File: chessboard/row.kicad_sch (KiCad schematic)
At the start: 15 parts, among them U1 PCA9548ADB

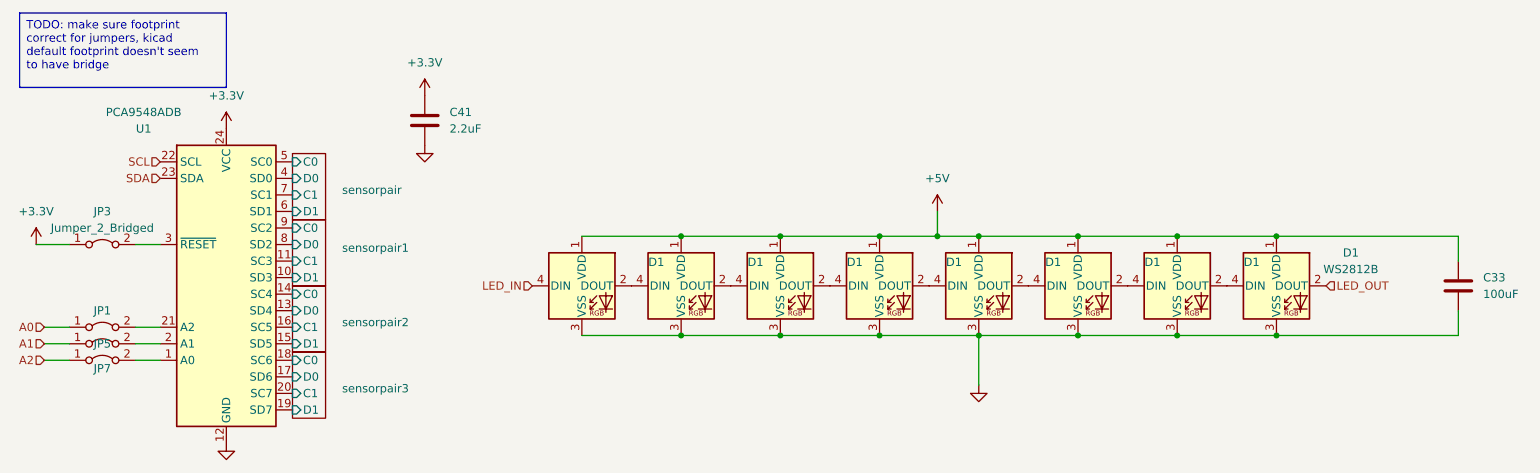
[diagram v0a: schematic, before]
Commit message: add some power logic, split chessboard and control board
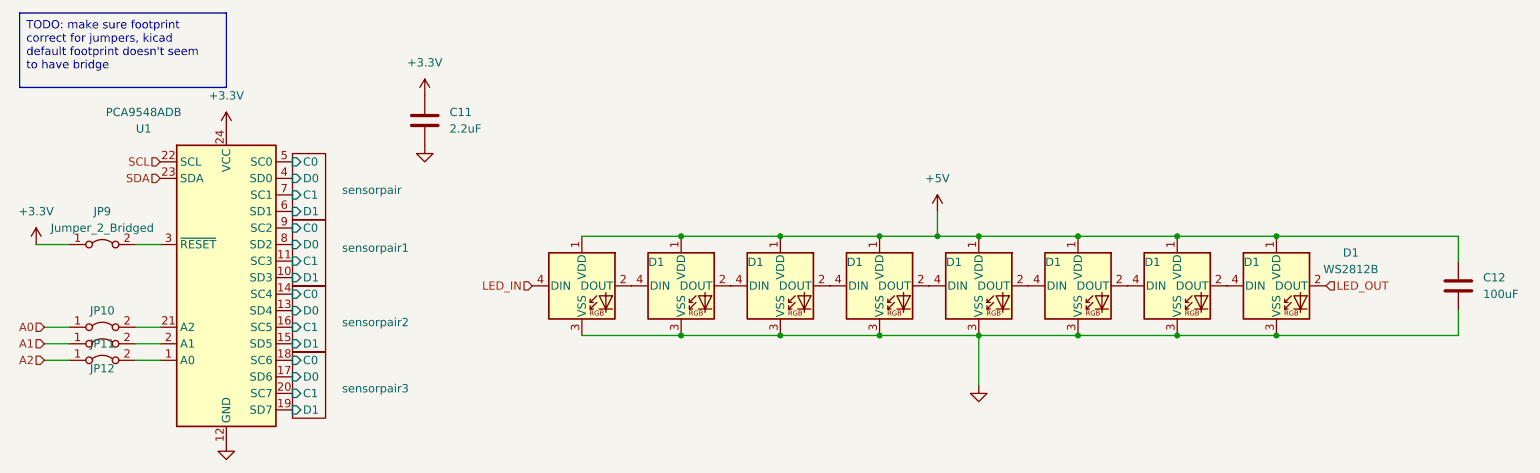
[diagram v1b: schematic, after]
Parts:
- renumbered C41 to C11, C33 to C12, JP1 to JP10, JP5 to JP11, JP7 to JP12, JP3 to JP9

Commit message: a
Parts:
- C3: renamed from C11; value 2.2uF -> 100nF; footprint (none) -> Capacitor_SMD:C_0805_2012Metric_Pad1.18x1.45mm_HandSolder
- C4: renamed from C12; value 100uF -> 22uF; footprint (none) -> Capacitor_SMD:C_0805_2012Metric_Pad1.18x1.45mm_HandSolder
- JP2: renamed from JP9; footprint (none) -> mylibrary:Bridged 2.5mm 1.0mm Test Points
- JP3: renamed from JP10; footprint (none) -> mylibrary:Bridged 2.5mm 1.0mm Test Points
- JP4: renamed from JP11; footprint (none) -> mylibrary:Bridged 2.5mm 1.0mm Test Points
- JP5: renamed from JP12; footprint (none) -> mylibrary:Bridged 2.5mm 1.0mm Test Points
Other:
- sheet sensorpair renamed sensorpair0

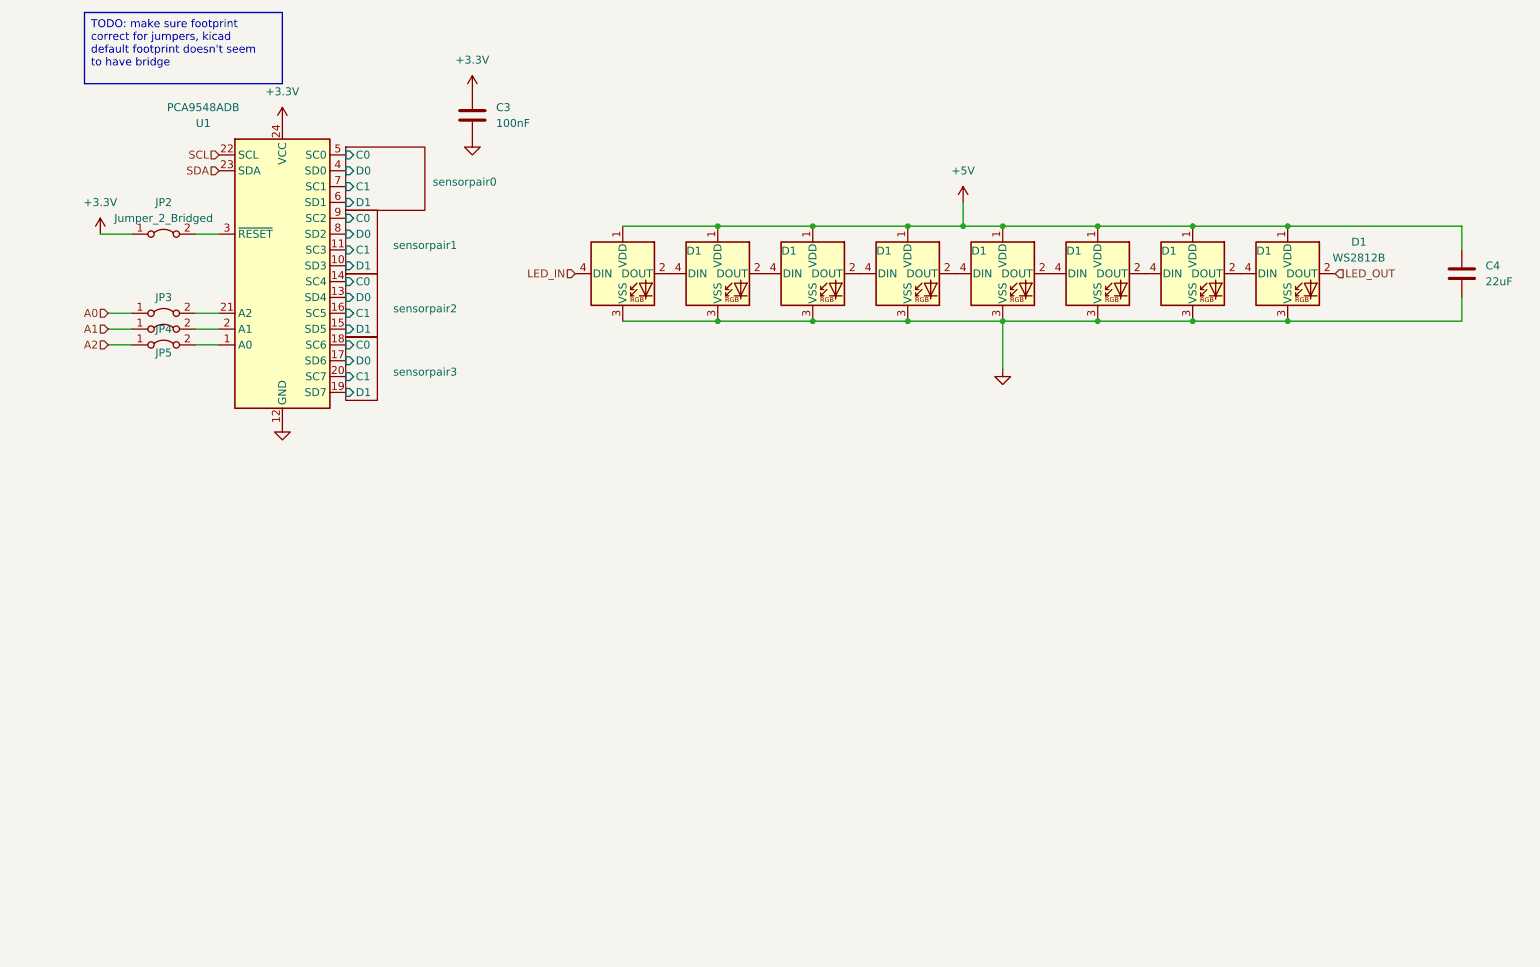
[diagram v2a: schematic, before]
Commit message: new single row board
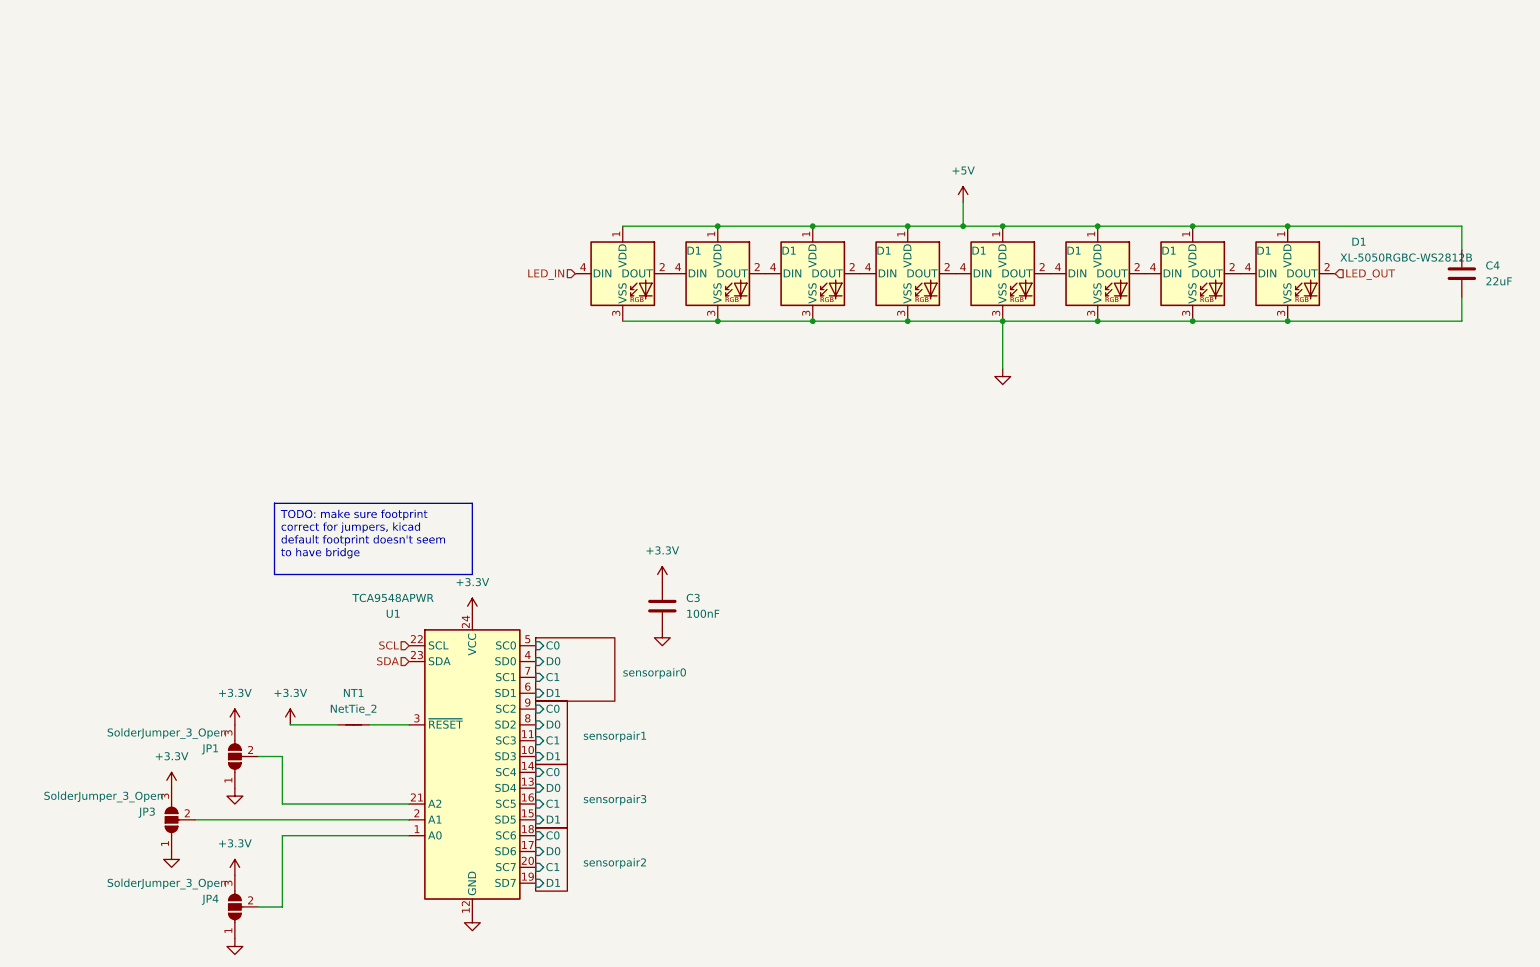
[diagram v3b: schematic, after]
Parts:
- removed JP2, JP3, JP4, JP5: Jumper_2_Bridged, mylibrary:Bridged 2.5mm 1.0mm Test Points, symbol Jumper:Jumper_2_Bridged
- added JP1, JP3, JP4: SolderJumper_3_Open, Jumper:SolderJumper-3_P2.0mm_Open_TrianglePad1.0x1.5mm, symbol Jumper:SolderJumper_3_Open
- added NT1: NetTie_2, Jumper:SolderJumper-2_P1.3mm_Bridged_Pad1.0x1.5mm, symbol Device:NetTie_2
- D1: value WS2812B -> XL-5050RGBC-WS2812B
- U1: value PCA9548ADB -> TCA9548APWR; footprint Package_SO:SSOP-24_5.3x8.2mm_P0.65mm -> Package_SO:TSSOP-24_4.4x7.8mm_P0.65mm
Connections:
- net +3.3V: now also JP1.3 (B), JP3.3 (B), JP4.3 (B), NT1.1
- net GND: now also JP1.1 (A), JP3.1 (A), JP4.1 (A)
- net sensorpair2/C0: now also U1.18 (SC6); no longer U1.14 (SC4)
- net sensorpair2/C1: now also U1.20 (SC7); no longer U1.16 (SC5)
- net sensorpair2/D0: now also U1.17 (SD6); no longer U1.13 (SD4)
- net sensorpair2/D1: now also U1.19 (SD7); no longer U1.15 (SD5)
- net sensorpair3/C0: now also U1.14 (SC4); no longer U1.18 (SC6)
- net sensorpair3/C1: now also U1.16 (SC5); no longer U1.20 (SC7)
- net sensorpair3/D0: now also U1.13 (SD4); no longer U1.17 (SD6)
- net sensorpair3/D1: now also U1.15 (SD5); no longer U1.19 (SD7)
- net at U1.1 (A0): now also JP4.2 (C)
- net at U1.2 (A1): now also JP3.2 (C)
- net at U1.21 (A2): now also JP1.2 (C)
- net at U1.3 (~{RESET}): now also NT1.2
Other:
- moved on the sheet: C3, U1

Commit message: make it pretty
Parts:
- renumbered C3 to C1, C4 to C2
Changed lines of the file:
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@@
   (symbol (lib_id "power:+3.3V") (at 120.65 116.84 0) (unit 1)
     (in_bom yes) (on_board yes) (dnp no) (fields_autoplaced)
-    (property "Reference" "#PWR037" (at 120.65 120.65 0)
+    (property "Reference" "#PWR019" (at 120.65 120.65 0)
       (effects (font (size 1.27 1.27)) hide)
     )
@@
   (symbol (lib_id "power:+3.3V") (at 90.17 121.92 0) (unit 1)
     (in_bom yes) (on_board yes) (dnp no) (fields_autoplaced)
-    (property "Reference" "#PWR035" (at 90.17 125.73 0)
+    (property "Reference" "#PWR017" (at 90.17 125.73 0)
       (effects (font (size 1.27 1.27)) hide)
     )
@@
   (symbol (lib_id "power:GND") (at 90.17 170.18 0) (unit 1)
     (in_bom yes) (on_board yes) (dnp no) (fields_autoplaced)
-    (property "Reference" "#PWR036" (at 90.17 176.53 0)
+    (property "Reference" "#PWR018" (at 90.17 176.53 0)
       (effects (font (size 1.27 1.27)) hide)
     )
@@
   (symbol (lib_id "power:+3.3V") (at 41.91 149.86 0) (unit 1)
     (in_bom yes) (on_board yes) (dnp no) (fields_autoplaced)
-    (property "Reference" "#PWR09" (at 41.91 153.67 0)
+    (property "Reference" "#PWR011" (at 41.91 153.67 0)
       (effects (font (size 1.27 1.27)) hide)
     )
@@
   (symbol (lib_id "power:GND") (at 120.65 124.46 0) (unit 1)
     (in_bom yes) (on_board yes) (dnp no) (fields_autoplaced)
-    (property "Reference" "#PWR038" (at 120.65 130.81 0)
+    (property "Reference" "#PWR020" (at 120.65 130.81 0)
       (effects (font (size 1.27 1.27)) hide)
     )
@@
   (symbol (lib_id "power:+5V") (at 168.91 55.88 0) (unit 1)
     (in_bom yes) (on_board yes) (dnp no) (fields_autoplaced)
-    (property "Reference" "#PWR039" (at 168.91 59.69 0)
+    (property "Reference" "#PWR021" (at 168.91 59.69 0)
       (effects (font (size 1.27 1.27)) hide)
     )
@@
   (symbol (lib_id "Device:C") (at 120.65 120.65 0) (unit 1)
     (in_bom yes) (on_board yes) (dnp no) (fields_autoplaced)
-    (property "Reference" "C3" (at 124.46 119.38 0)
+    (property "Reference" "C1" (at 124.46 119.38 0)
       (effects (font (size 1.27 1.27)) (justify left))
     )
@@
   (symbol (lib_id "power:+3.3V") (at 52.07 139.7 0) (unit 1)
     (in_bom yes) (on_board yes) (dnp no) (fields_autoplaced)
-    (property "Reference" "#PWR011" (at 52.07 143.51 0)
+    (property "Reference" "#PWR09" (at 52.07 143.51 0)
       (effects (font (size 1.27 1.27)) hide)
     )
@@
   (symbol (lib_id "Device:C") (at 248.92 67.31 0) (unit 1)
     (in_bom yes) (on_board yes) (dnp no) (fields_autoplaced)
-    (property "Reference" "C4" (at 252.73 66.04 0)
+    (property "Reference" "C2" (at 252.73 66.04 0)
       (effects (font (size 1.27 1.27)) (justify left))
     )
@@
   (symbol (lib_id "power:+3.3V") (at 60.96 139.7 0) (unit 1)
     (in_bom yes) (on_board yes) (dnp no) (fields_autoplaced)
-    (property "Reference" "#PWR034" (at 60.96 143.51 0)
+    (property "Reference" "#PWR016" (at 60.96 143.51 0)
       (effects (font (size 1.27 1.27)) hide)
     )
@@
   (symbol (lib_id "power:GND") (at 175.26 82.55 0) (unit 1)
     (in_bom yes) (on_board yes) (dnp no) (fields_autoplaced)
-    (property "Reference" "#PWR040" (at 175.26 88.9 0)
-      (effects (font (size 1.27 1.27)) hide)
-    )
+    (property "Reference" "#PWR022" (at 175.26 88.9 0)
+      (effects (font (size 1.27 1.27)) hide)
+    )

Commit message: ready to buy
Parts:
- removed NT1: NetTie_2, Jumper:SolderJumper-2_P1.3mm_Bridged_Pad1.0x1.5mm, symbol Device:NetTie_2
- added JP5: SolderJumper_2_Open, Jumper:SolderJumper-2_P1.3mm_Open_Pad1.0x1.5mm, symbol Jumper:SolderJumper_2_Open
- added R1: 10k, Resistor_SMD:R_0805_2012Metric_Pad1.20x1.40mm_HandSolder, symbol Device:R
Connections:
- net +3.3V: now also R1.1
- net GND: now also JP5.1 (A)
- net at U1.3 (~{RESET}): now also JP5.2 (B), R1.2
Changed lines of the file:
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@@
   (junction (at 160.02 74.93) (diameter 0) (color 0 0 0 0)
   )
+  (junction (at 74.93 139.7) (diameter 0) (color 0 0 0 0)
+  )
   (junction (at 220.98 59.69) (diameter 0) (color 0 0 0 0)
   )
@@
     (stroke (width 0) (type default))
   )
-  (wire (pts (xy 73.66 139.7) (xy 80.01 139.7))
+  (wire (pts (xy 73.66 139.7) (xy 74.93 139.7))
     (stroke (width 0) (type default))
   )
@@
     (stroke (width 0) (type default))
   )
+  (wire (pts (xy 74.93 139.7) (xy 80.01 139.7))
+    (stroke (width 0) (type default))
+  )
   (wire (pts (xy 190.5 59.69) (xy 205.74 59.69))
     (stroke (width 0) (type default))
@@
     (stroke (width 0) (type default))
   )
-  (wire (pts (xy 60.96 139.7) (xy 68.58 139.7))
+  (wire (pts (xy 60.96 139.7) (xy 66.04 139.7))
     (stroke (width 0) (type default))
   )
@@
     )
   )
-  (symbol (lib_id "Device:NetTie_2") (at 71.12 139.7 0) (unit 1)
-    (in_bom no) (on_board yes) (dnp no) (fields_autoplaced)
-    (property "Reference" "NT1" (at 71.12 134.62 0)
-      (effects (font (size 1.27 1.27)))
-    )
-    (property "Value" "NetTie_2" (at 71.12 137.16 0)
-      (effects (font (size 1.27 1.27)))
-    )
-    (property "Footprint" "Jumper:SolderJumper-2_P1.3mm_Bridged_Pad1.0x1.5mm" (at 71.12 139.7 0)
-      (effects (font (size 1.27 1.27)) hide)
-    )
-    (property "Datasheet" "~" (at 71.12 139.7 0)
-      (effects (font (size 1.27 1.27)) hide)
-    )
-    (pin "1")
-    (pin "2")
-    (instances
-      (project "chessboard"
-        (path "/178674ef-da23-4447-9d4b-ea3429461404/501c11bc-04bd-4d54-8bc8-c6f63ce2a0b8"
-          (reference "NT1") (unit 1)
+  (symbol (lib_id "Device:R") (at 69.85 139.7 90) (unit 1)
+    (in_bom yes) (on_board yes) (dnp no) (fields_autoplaced)
+    (property "Reference" "R1" (at 69.85 133.35 90)
+      (effects (font (size 1.27 1.27)))
+    )
+    (property "Value" "10k" (at 69.85 135.89 90)
+      (effects (font (size 1.27 1.27)))
+    )
+    (property "Footprint" "Resistor_SMD:R_0805_2012Metric_Pad1.20x1.40mm_HandSolder" (at 69.85 141.478 90)
+      (effects (font (size 1.27 1.27)) hide)
+    )
+    (property "Datasheet" "~" (at 69.85 139.7 0)
+      (effects (font (size 1.27 1.27)) hide)
+    )
+    (pin "1")
+    (pin "2")
+    (instances
+      (project "chessboard"
+        (path "/178674ef-da23-4447-9d4b-ea3429461404/501c11bc-04bd-4d54-8bc8-c6f63ce2a0b8"
+          (reference "R1") (unit 1)
         )
       )
@@
     )
   )
+  (symbol (lib_id "power:GND") (at 74.93 147.32 0) (unit 1)
+    (in_bom yes) (on_board yes) (dnp no) (fields_autoplaced)
+    (property "Reference" "#PWR010" (at 74.93 153.67 0)
+      (effects (font (size 1.27 1.27)) hide)
+    )
+    (property "Value" "GND" (at 74.93 152.4 0)
+      (effects (font (size 1.27 1.27)) hide)
+    )
+    (property "Footprint" "" (at 74.93 147.32 0)
+      (effects (font (size 1.27 1.27)) hide)
+    )
+    (property "Datasheet" "" (at 74.93 147.32 0)
+      (effects (font (size 1.27 1.27)) hide)
+    )
+    (pin "1")
+    (instances
+      (project "chessboard"
+        (path "/178674ef-da23-4447-9d4b-ea3429461404"
+          (reference "#PWR010") (unit 1)
+        )
+        (path "/178674ef-da23-4447-9d4b-ea3429461404/501c11bc-04bd-4d54-8bc8-c6f63ce2a0b8"
+          (reference "#PWR042") (unit 1)
+        )
+      )
+    )
+  )
   (symbol (lib_id "power:GND") (at 41.91 160.02 0) (unit 1)
     (in_bom yes) (on_board yes) (dnp no) (fields_autoplaced)
@@
         )
       )
+    )
+  )
+  (symbol (lib_id "Jumper:SolderJumper_2_Open") (at 74.93 143.51 270) (mirror x) (unit 1)
+    (in_bom yes) (on_board yes) (dnp no)
+    (property "Reference" "JP5" (at 77.47 142.24 90)
+      (effects (font (size 1.27 1.27)) (justify left))
+    )
+    (property "Value" "SolderJumper_2_Open" (at 63.5 144.78 90)
+      (effects (font (size 1.27 1.27)) (justify left))
+    )
+    (property "Footprint" "Jumper:SolderJumper-2_P1.3mm_Open_Pad1.0x1.5mm" (at 74.93 143.51 0)
+      (effects (font (size 1.27 1.27)) hide)
+    )
+    (property "Datasheet" "~" (at 74.93 143.51 0)
+      (effects (font (size 1.27 1.27)) hide)
+    )
+    (pin "2")
+    (pin "1")
+    (instances
+      (project "chessboard"
+        (path "/178674ef-da23-4447-9d4b-ea3429461404/501c11bc-04bd-4d54-8bc8-c6f63ce2a0b8"
+          (reference "JP5") (unit 1)
+        )
+      )
